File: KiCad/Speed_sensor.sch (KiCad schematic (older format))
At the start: 22 parts

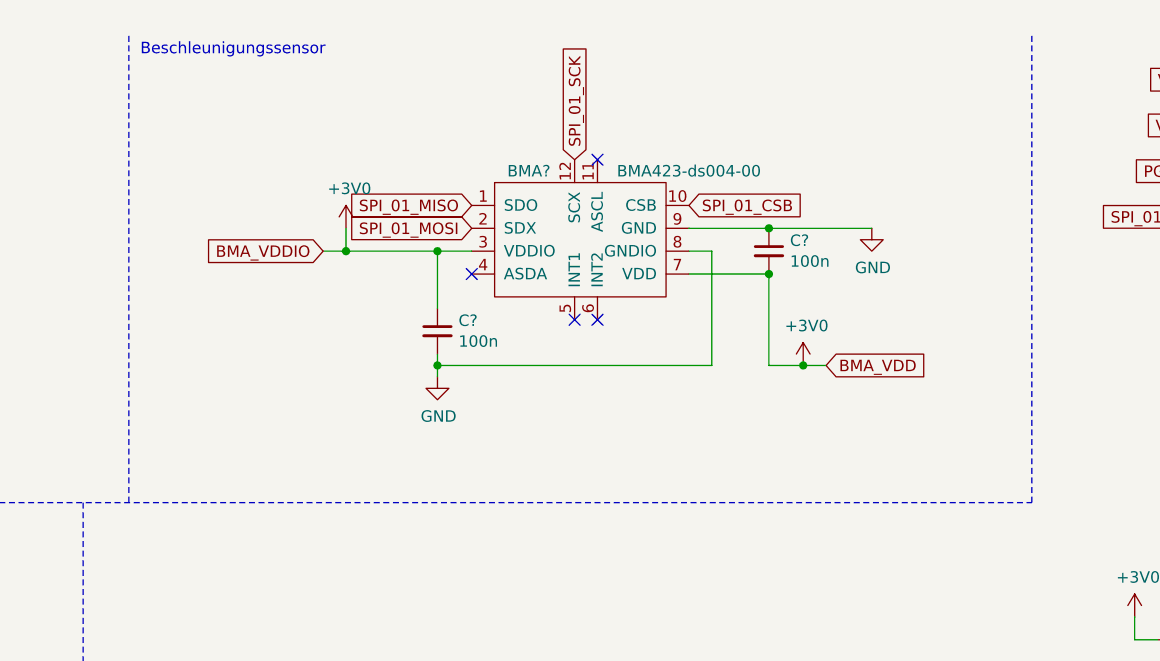
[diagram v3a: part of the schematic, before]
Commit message: int pins am BMA hinzugefügt (aber noch nicht an nrf angeschlossen
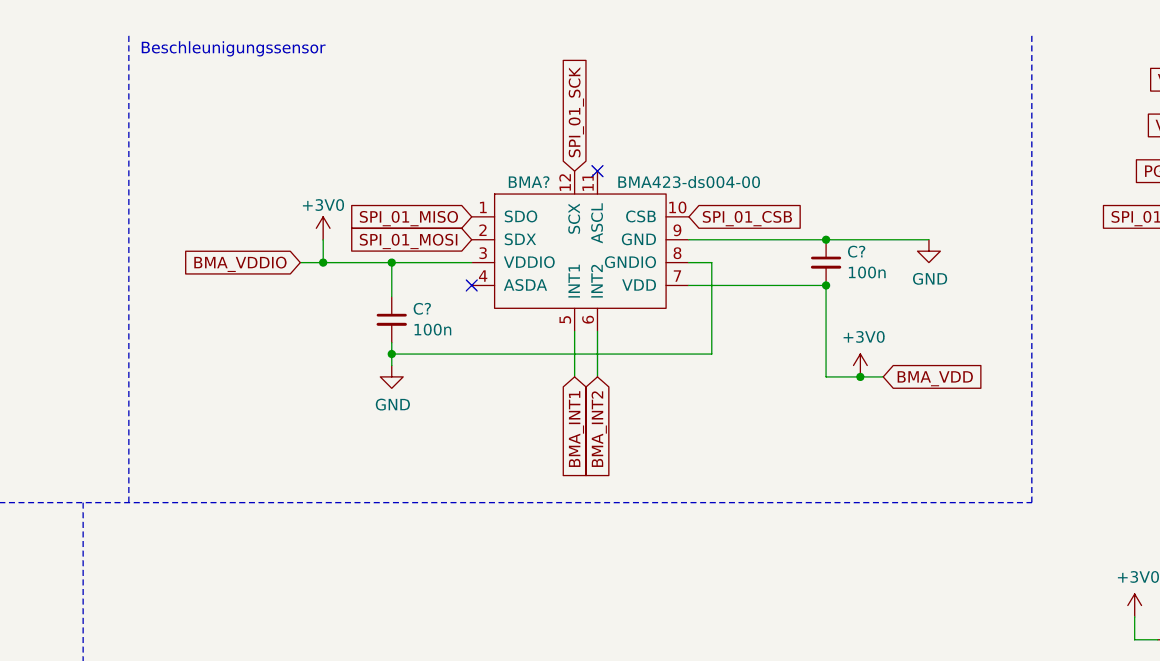
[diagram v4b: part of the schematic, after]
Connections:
- net BMA_INT1: now reaches BMA?.5 (INT1)
- net BMA_INT2: now reaches BMA?.6 (INT2)
- no-connect marks 7 -> 5
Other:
- moved on the sheet: BMA?, C?
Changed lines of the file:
@@
 L Nils_KiCADLibrary:BMA423-ds004-00 BMA?
 U 1 1 609CB726
-P 7350 1400
-F 0 "BMA?" H 7100 1700 50  0000 C CNN
-F 1 "BMA423-ds004-00" H 7800 1700 50  0000 C CNN
-F 2 "" H 7350 1300 50  0001 C CNN
-F 3 "" H 7350 1300 50  0001 C CNN
-	1    7350 1400
+P 7350 1450
+F 0 "BMA?" H 7100 1750 50  0000 C CNN
+F 1 "BMA423-ds004-00" H 7800 1750 50  0000 C CNN
+F 2 "" H 7350 1350 50  0001 C CNN
+F 3 "" H 7350 1350 50  0001 C CNN
+	1    7350 1450
 	1    0    0    -1
 $EndComp
@@
 L Device:C_Small C?
 U 1 1 609CE9BE
-P 6700 1800
-F 0 "C?" H 6792 1846 50  0000 L CNN
-F 1 "100n" H 6792 1755 50  0000 L CNN
-F 2 "" H 6700 1800 50  0001 C CNN
-F 3 "~" H 6700 1800 50  0001 C CNN
-	1    6700 1800
+P 6500 1750
+F 0 "C?" H 6592 1796 50  0000 L CNN
+F 1 "100n" H 6592 1705 50  0000 L CNN
+F 2 "" H 6500 1750 50  0001 C CNN
+F 3 "~" H 6500 1750 50  0001 C CNN
+	1    6500 1750
 	1    0    0    -1
 $EndComp
@@
 L Device:C_Small C?
 U 1 1 609CF366
-P 8150 1450
-F 0 "C?" H 8242 1496 50  0000 L CNN
-F 1 "100n" H 8242 1405 50  0000 L CNN
-F 2 "" H 8150 1450 50  0001 C CNN
-F 3 "~" H 8150 1450 50  0001 C CNN
-	1    8150 1450
+P 8400 1500
+F 0 "C?" H 8492 1546 50  0000 L CNN
+F 1 "100n" H 8492 1455 50  0000 L CNN
+F 2 "" H 8400 1500 50  0001 C CNN
+F 3 "~" H 8400 1500 50  0001 C CNN
+	1    8400 1500
 	1    0    0    -1
 $EndComp
@@
 L power:GND #PWR0115
 U 1 1 609D033F
-P 6700 2000
-F 0 "#PWR0115" H 6700 1750 50  0001 C CNN
-F 1 "GND" H 6705 1827 50  0000 C CNN
-F 2 "" H 6700 2000 50  0001 C CNN
-F 3 "" H 6700 2000 50  0001 C CNN
-	1    6700 2000
+P 6500 1950
+F 0 "#PWR0115" H 6500 1700 50  0001 C CNN
+F 1 "GND" H 6505 1777 50  0000 C CNN
+F 2 "" H 6500 1950 50  0001 C CNN
+F 3 "" H 6500 1950 50  0001 C CNN
+	1    6500 1950
 	1    0    0    -1
 $EndComp
@@
 L power:GND #PWR0116
 U 1 1 609D18BF
-P 8600 1350
-F 0 "#PWR0116" H 8600 1100 50  0001 C CNN
-F 1 "GND" H 8605 1177 50  0000 C CNN
-F 2 "" H 8600 1350 50  0001 C CNN
-F 3 "" H 8600 1350 50  0001 C CNN
-	1    8600 1350
-	1    0    0    -1
-$EndComp
-Connection ~ 8150 1350
-Wire Wire Line
-	8150 1350 7800 1350
-Wire Wire Line
-	7800 1450 7900 1450
-Wire Wire Line
-	6700 1700 6700 1450
-Wire Wire Line
-	6700 1450 6850 1450
-Wire Wire Line
-	7800 1550 8150 1550
-Text GLabel 8400 1950 2    50   Input ~ 0
+P 8850 1400
+F 0 "#PWR0116" H 8850 1150 50  0001 C CNN
+F 1 "GND" H 8855 1227 50  0000 C CNN
+F 2 "" H 8850 1400 50  0001 C CNN
+F 3 "" H 8850 1400 50  0001 C CNN
+	1    8850 1400
+	1    0    0    -1
+$EndComp
+Connection ~ 8400 1400
+Text GLabel 8650 2000 2    50   Input ~ 0
 BMA_VDD
-Connection ~ 8150 1550
-Text GLabel 6200 1450 0    50   Input ~ 0
+Connection ~ 8400 1600
+Text GLabel 6100 1500 0    50   Input ~ 0
 BMA_VDDIO
-Connection ~ 6700 1450
-NoConn ~ 7400 1050
-NoConn ~ 6850 1550
-Wire Wire Line
-	6700 1900 6700 1950
-Connection ~ 6700 1950
-Wire Wire Line
-	6700 1950 6700 2000
+NoConn ~ 7400 1100
+NoConn ~ 6850 1600
 Text GLabel 3800 4250 2    50   Input ~ 0
 SPI_01_CSB
@@
 Text Notes 5400 600  0    50   ~ 0
 Beschleunigungssensor
-NoConn ~ 7300 1750
-NoConn ~ 7400 1750
-Wire Wire Line
-	7900 1950 7900 1450
-Wire Wire Line
-	6700 1950 7900 1950
-Wire Wire Line
-	6200 1450 6300 1450
-Wire Wire Line
-	6300 1450 6300 1350
-Connection ~ 6300 1450
-Wire Wire Line
-	6300 1450 6700 1450
-Wire Wire Line
-	8150 1550 8150 1950
-Wire Wire Line
-	8150 1350 8600 1350
+Wire Wire Line
+	6100 1500 6200 1500
+Wire Wire Line
+	6200 1500 6200 1400
+Connection ~ 6200 1500
+Wire Wire Line
+	8400 1600 8400 2000
+Wire Wire Line
+	8400 1400 8850 1400
 $Comp
 L Connector_Generic:Conn_02x05_Odd_Even J?
@@
 L power:+3V0 #PWR0121
 U 1 1 60889DED
-P 6300 1350
-F 0 "#PWR0121" H 6300 1200 50  0001 C CNN
-F 1 "+3V0" H 6315 1523 50  0000 C CNN
-F 2 "" H 6300 1350 50  0001 C CNN
-F 3 "" H 6300 1350 50  0001 C CNN
-	1    6300 1350
+P 6200 1400
+F 0 "#PWR0121" H 6200 1250 50  0001 C CNN
+F 1 "+3V0" H 6200 1550 50  0000 C CNN
+F 2 "" H 6200 1400 50  0001 C CNN
+F 3 "" H 6200 1400 50  0001 C CNN
+	1    6200 1400
 	1    0    0    -1
 $EndComp
@@
 L power:+3V0 #PWR0122
 U 1 1 6088A223
-P 8300 1950
-F 0 "#PWR0122" H 8300 1800 50  0001 C CNN
-F 1 "+3V0" H 8315 2123 50  0000 C CNN
-F 2 "" H 8300 1950 50  0001 C CNN
-F 3 "" H 8300 1950 50  0001 C CNN
-	1    8300 1950
+P 8550 2000
+F 0 "#PWR0122" H 8550 1850 50  0001 C CNN
+F 1 "+3V0" H 8565 2173 50  0000 C CNN
+F 2 "" H 8550 2000 50  0001 C CNN
+F 3 "" H 8550 2000 50  0001 C CNN
+	1    8550 2000
 	1    0    0    -1
 $EndComp
@@
 $EndComp
 Wire Wire Line
-	8150 1950 8300 1950
-Connection ~ 8300 1950
-Wire Wire Line
-	8300 1950 8400 1950
+	8400 2000 8550 2000
+Connection ~ 8550 2000
+Wire Wire Line
+	8550 2000 8650 2000
 Wire Wire Line
 	2700 3500 2700 4050
@@
 	0    1    1    0
 $EndComp
-Text GLabel 7800 1250 2    50   Input ~ 0
+Text GLabel 7800 1300 2    50   Input ~ 0
 SPI_01_CSB
 Text GLabel 10100 1300 0    50   Input ~ 0
 SPI_01_CSB
-Text GLabel 7300 1050 1    50   Input ~ 0
+Text GLabel 7300 1100 1    50   Input ~ 0
 SPI_01_SCK
 Text GLabel 3800 4750 2    50   Input ~ 0
 SPI_01_SCK
-Text GLabel 6850 1250 0    50   Input ~ 0
+Text GLabel 6850 1300 0    50   Input ~ 0
 SPI_01_MISO
-Text GLabel 6850 1350 0    50   Input ~ 0
+Text GLabel 6850 1400 0    50   Input ~ 0
 SPI_01_MOSI
+Text GLabel 7300 2000 3    50   Input ~ 0
+BMA_INT1
+Text GLabel 7400 2000 3    50   Input ~ 0
+BMA_INT2
+Wire Wire Line
+	6500 1850 6500 1900
+Wire Wire Line
+	7800 1600 8400 1600
+Wire Wire Line
+	7800 1400 8400 1400
+Wire Wire Line
+	6200 1500 6500 1500
+Wire Wire Line
+	6500 1650 6500 1500
+Connection ~ 6500 1500
+Wire Wire Line
+	6500 1500 6850 1500
+Wire Wire Line
+	7800 1500 7900 1500
+Wire Wire Line
+	7900 1500 7900 1900
+Wire Wire Line
+	7900 1900 6500 1900
+Connection ~ 6500 1900
+Wire Wire Line
+	6500 1900 6500 1950
+Wire Wire Line
+	7300 2000 7300 1800
+Wire Wire Line
+	7400 1800 7400 2000
 $EndSCHEMATC

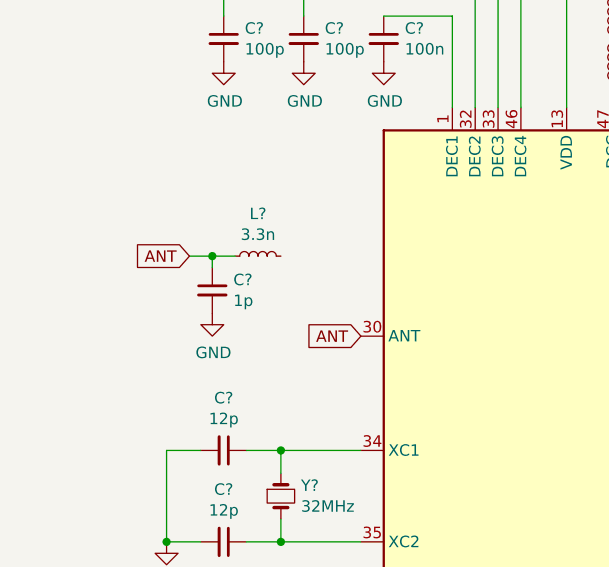
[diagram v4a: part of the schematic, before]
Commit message: ANT bauteile vom nrf entfernt
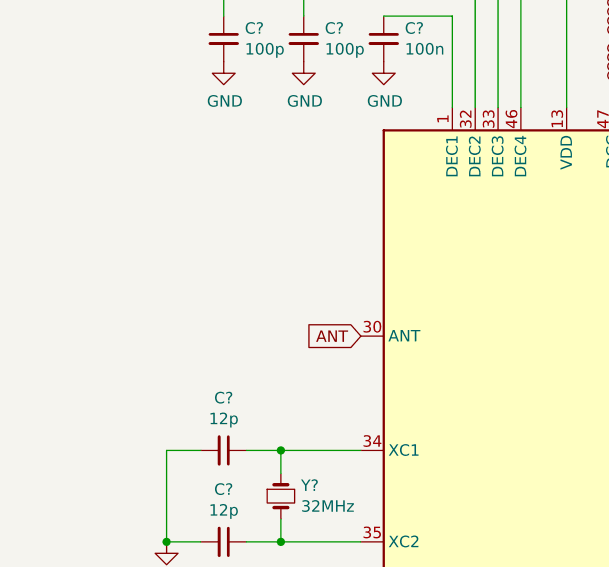
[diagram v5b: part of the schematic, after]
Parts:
- removed C?: 1p, symbol Device:C_Small
- removed L?: 3.3n, symbol Device:L_Small
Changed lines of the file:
@@
 Connection ~ 2900 2850
-$Comp
-L Device:L_Small L?
-U 1 1 60848098
-P 1550 4700
-F 0 "L?" V 1735 4700 50  0000 C CNN
-F 1 "3.3n" V 1644 4700 50  0000 C CNN
-F 2 "" H 1550 4700 50  0001 C CNN
-F 3 "~" H 1550 4700 50  0001 C CNN
-	1    1550 4700
-	0    -1   -1   0
-$EndComp
-$Comp
-L Device:C_Small C?
-U 1 1 6084886D
-P 1350 4850
-F 0 "C?" H 1442 4896 50  0000 L CNN
-F 1 "1p" H 1442 4805 50  0000 L CNN
-F 2 "" H 1350 4850 50  0001 C CNN
-F 3 "~" H 1350 4850 50  0001 C CNN
-	1    1350 4850
-	1    0    0    -1
-$EndComp
-$Comp
-L power:GND #PWR0105
-U 1 1 60849106
-P 1350 4950
-F 0 "#PWR0105" H 1350 4700 50  0001 C CNN
-F 1 "GND" H 1355 4777 50  0000 C CNN
-F 2 "" H 1350 4950 50  0001 C CNN
-F 3 "" H 1350 4950 50  0001 C CNN
-	1    1350 4950
-	1    0    0    -1
-$EndComp
 $Comp
 L Device:Crystal_Small Y?
@@
 Text GLabel 2000 5050 0    50   Input ~ 0
 ANT
-Text GLabel 1250 4700 0    50   Input ~ 0
-ANT
-Wire Wire Line
-	1450 4700 1350 4700
-Wire Wire Line
-	1350 4750 1350 4700
-Connection ~ 1350 4700
-Wire Wire Line
-	1350 4700 1250 4700
 Wire Notes Line
 	5150 2550 5150 7750

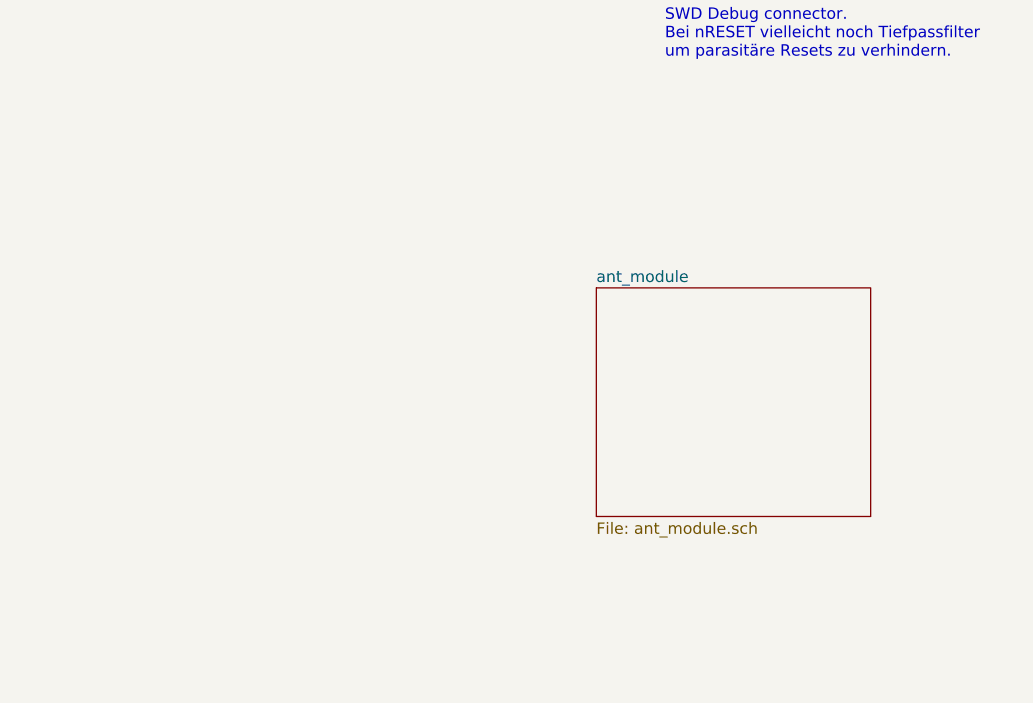
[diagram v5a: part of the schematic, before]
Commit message: Kommentar zum ANT Modul
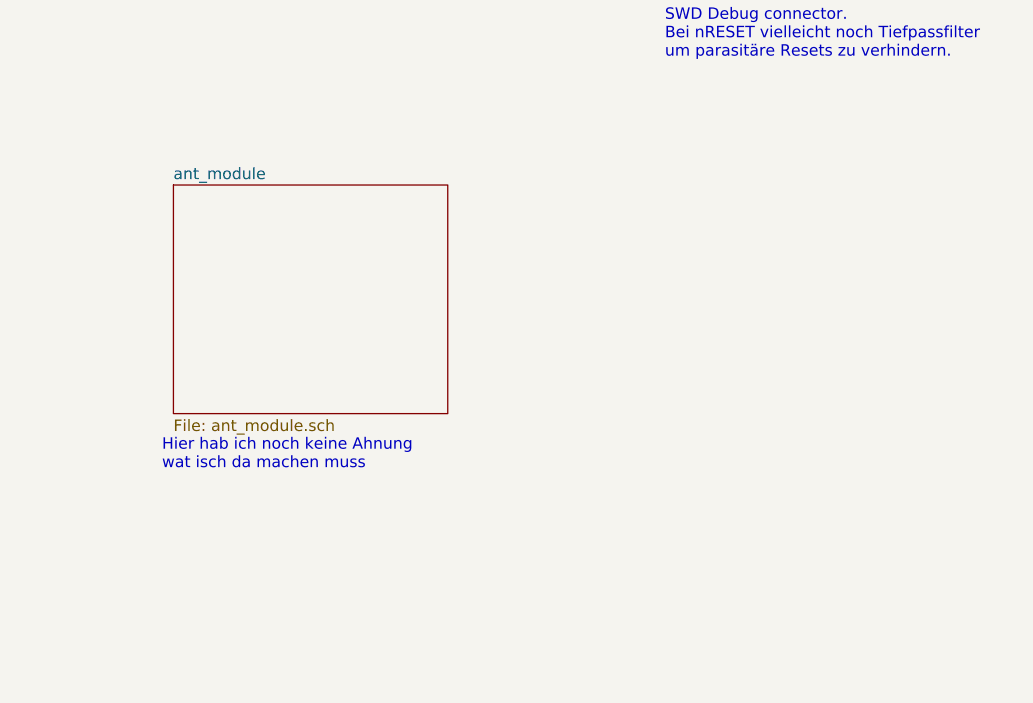
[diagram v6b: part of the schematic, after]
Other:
- note added: "Hier hab ich noch keine Ahnung \nwat isch da machen muss"
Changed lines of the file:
@@
 encoding utf-8
 Sheet 1 3
-Title ""
-Date ""
-Rev ""
+Title "Speed Sensor"
+Date "2021-04-27"
+Rev "1.0"
 Comp ""
 Comment1 ""
@@
 	3100 3950 3100 4050
 $Sheet
-S 9300 5150 1200 1000
+S 7450 4700 1200 1000
 U 6087B1AF
 F0 "ant_module" 50
@@
 Wire Wire Line
 	7400 1800 7400 2000
+Text Notes 7400 5950 0    50   ~ 0
+Hier hab ich noch keine Ahnung \nwat isch da machen muss
 $EndSCHEMATC

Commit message: paar Sachen mit Manu angepasst
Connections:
- net BMA_INT1: now also U?.29 (P0.24)
- net BMA_INT2: now also U?.28 (P0.23)
- net SPI_01_CSB: now also U?.16 (P0.13); no longer U?.2 (P0.00/XL1)
- net SPI_01_MISO: now also U?.17 (P0.14); no longer U?.8 (P0.06)
- net SPI_01_MOSI: now also U?.19 (P0.16); no longer U?.10 (P0.08)
- net SPI_01_SCK: now also U?.18 (P0.15); no longer U?.7 (P0.05/AIN3)
- net SWO: now reaches U?.21 (P0.18/SWO)
- net SWO: now also J?.6 (Pin_6)
- net nRESET renamed ~RESET~
- no-connect marks 5 -> 4
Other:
- note added: "den hier brauch ich!"
- note removed: "Hier hab ich noch keine Ahnung \nwat isch da machen muss"
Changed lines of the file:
@@
 NoConn ~ 7400 1100
 NoConn ~ 6850 1600
-Text GLabel 3800 4250 2    50   Input ~ 0
+Text GLabel 3800 5550 2    50   Input ~ 0
 SPI_01_CSB
-Text GLabel 3800 4850 2    50   Input ~ 0
+Text GLabel 3800 5650 2    50   Input ~ 0
 SPI_01_MISO
-Text GLabel 3800 5050 2    50   Input ~ 0
+Text GLabel 3800 5850 2    50   Input ~ 0
 SPI_01_MOSI
 Wire Notes Line
@@
 NoConn ~ 9850 3450
 Text GLabel 2000 6350 0    50   Input ~ 0
-nRESET
+~RESET~
 Text GLabel 10350 3550 2    50   Input ~ 0
-nRESET
-NoConn ~ 10350 3350
+~RESET~
 Text Notes 9600 4150 0    50   ~ 0
 SWD Debug connector.\nBei nRESET vielleicht noch Tiefpassfilter\num parasitäre Resets zu verhindern.
@@
 Wire Wire Line
 	3100 3950 3100 4050
-$Sheet
-S 7450 4700 1200 1000
-U 6087B1AF
-F0 "ant_module" 50
-F1 "ant_module.sch" 50
-$EndSheet
 Wire Notes Line
 	500  2550 9300 2550
@@
 Text GLabel 7300 1100 1    50   Input ~ 0
 SPI_01_SCK
-Text GLabel 3800 4750 2    50   Input ~ 0
+Text GLabel 3800 5750 2    50   Input ~ 0
 SPI_01_SCK
 Text GLabel 6850 1300 0    50   Input ~ 0
@@
 Wire Wire Line
 	7400 1800 7400 2000
-Text Notes 7400 5950 0    50   ~ 0
-Hier hab ich noch keine Ahnung \nwat isch da machen muss
+Text GLabel 3800 6550 2    50   Input ~ 0
+BMA_INT1
+Text GLabel 3800 6450 2    50   Input ~ 0
+BMA_INT2
+Text GLabel 3800 6050 2    50   Input ~ 0
+SWO
+Text GLabel 10350 3350 2    50   Input ~ 0
+SWO
+Text Notes 3850 4300 0    50   ~ 0
+den hier brauch ich!
 $EndSCHEMATC
